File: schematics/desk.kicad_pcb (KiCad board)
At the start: 2 copper layers, 88 x 123 mm, 34 parts, among them K1 energized = UP (raises desk), K2 energized = DOWN (lowers desk), Q1 IRLZ44N, Q2 2N7000, Q3 2N7000, Q4 BC337, Q5 BC327, U1 LM2596HV 29V-5V, U2 ESP32_DevKitC, U3 74HC123 250ms, U5 ACS724xLCTR-05AB, U6 74HC08

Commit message: Shorten the bottom further: fix U5's inflated bounding box
Same bug as U2 had: U5's Value text ("ACS724xLCTR-05AB") was rotated
90 degrees and long enough to stretch its bounding box to 15.3mm tall,
when the real component (per its courtyard) is only ~3.6mm. This
introduced itself when I rotated U5 as a whole footprint earlier to
shrink cluster height - the rotation carried its text along for the
ride without me checking where the text landed afterward.

Un-rotated the value text, shrunk it slightly, and moved it to sit
under the part instead of trailing off below it. That row's height
bottleneck moves to R4/R5 (12.3mm) instead of U5 (15.3mm before this
fix) - the tallest item in that row drops by ~3mm, so the board
outline follows: bottom edge trimmed from 123mm to 120mm.

No re-routing needed - the closest existing track stayed well clear
of the new edge (max track y 116.6mm vs new 120mm edge). Just moved
the board outline and both ground zone boundaries to match, then
refilled. Same 30 expected DRC items as before (28 intentional
isolated-copper + 2 thermal-relief), 0 unconnected.

Worth a systematic check of every footprint's bounding box against
its courtyard if further compaction is wanted - this is the second
instance of the same failure mode (U2 was the first), and a handful
of other parts show smaller versions of it that weren't worth chasing
here (normal reference/value label margin, not a rotation artifact).
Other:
- board size 88 x 123 mm -> 88 x 120 mm
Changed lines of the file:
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@@
 		)
 		(property "Value" "ACS724xLCTR-05AB"
-			(at 0 20.55 90)
+			(at -4.754 8.9453 0)
 			(layer "F.Fab")
 			(effects
 				(font
-					(size 1 1)
+					(size 0.8 0.8)
 					(thickness 0.15)
 				)
@@
 	)
 	(gr_line
-		(start 0 123)
+		(start 0 120)
 		(end 0 0)
 		(stroke
@@
 	(gr_line
 		(start 88 0)
-		(end 88 123)
+		(end 88 120)
 		(stroke
 			(width 0.1)
@@
 	)
 	(gr_line
-		(start 88 123)
-		(end 0 123)
+		(start 88 120)
+		(end 0 120)
 		(stroke
 			(width 0.1)
@@
 		(polygon
 			(pts
-				(xy 2 2) (xy 86 2) (xy 86 121) (xy 2 121)
+				(xy 2 2) (xy 86 2) (xy 86 118) (xy 2 118)
 			)
 		)
@@
 		(polygon
 			(pts
-				(xy 2 2) (xy 86 2) (xy 86 121) (xy 2 121)
+				(xy 2 2) (xy 86 2) (xy 86 118) (xy 2 118)
 			)
 		)

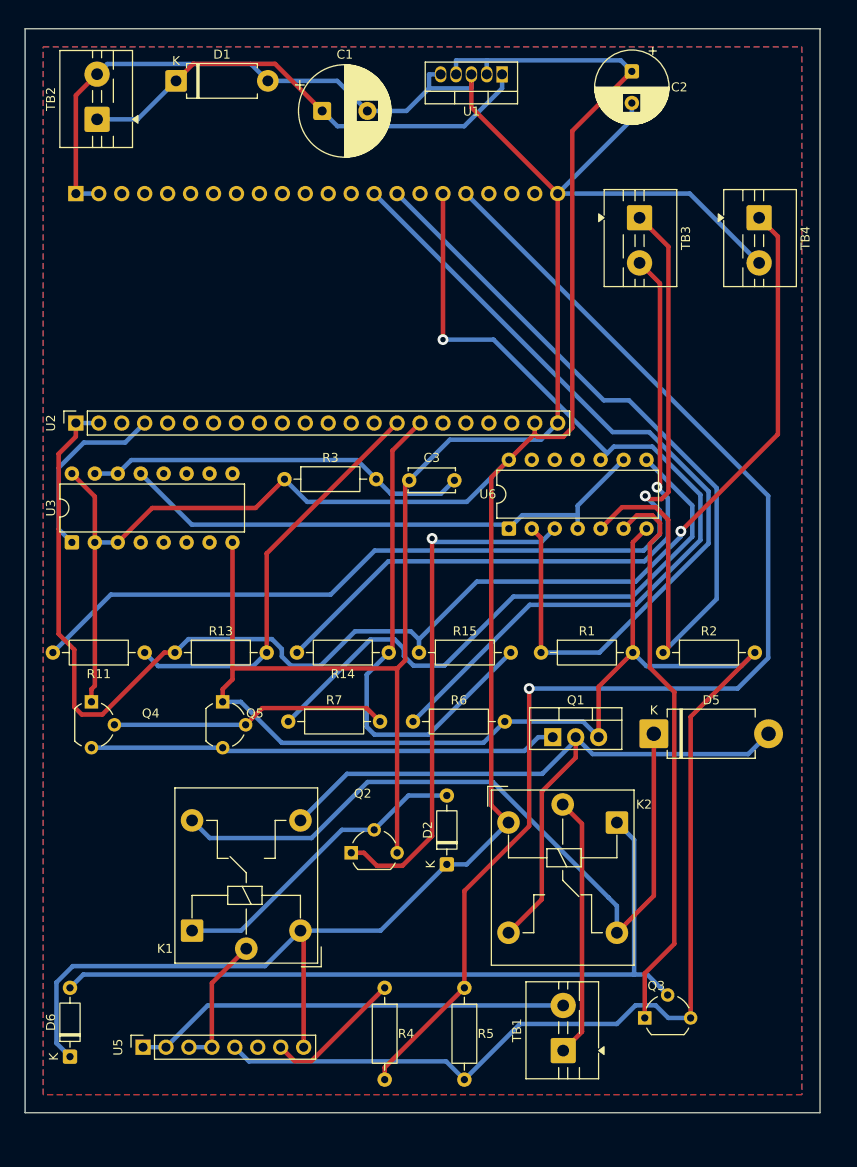
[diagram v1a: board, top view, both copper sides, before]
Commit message: Give R11 more edge clearance, clean up U3's label overhang
R11's left leg copper sat only 2.275mm from the board edge - the
tightest of any part on the board (everything else on the left margin
had 4mm+). Every other part in that row (R11/R13/R14/R15/R1/R2) had
6.2mm of unused width to its right before the board edge, so shifted
the whole row 1.7mm right: R11 now has 3.975mm of clearance, matching
the rest of the board, at zero cost to the layout.

Also did the full sweep for the U2/U5 text-overhang bug across every
footprint. Found one more real case (U3's "74HC123 250ms" value,
rotated 90 degrees, 12.8mm vs a 9.8mm courtyard) and cleaned it up,
though it doesn't change the board outline - U6 (18mm) is still the
taller item in that row. TB1-TB4's rotated "X pair" values looked
similar at a glance but turned out fine on inspection (bbox barely
exceeds their courtyard). Everything else's overhang is normal
reference/value label margin, not the rotation artifact.

Re-routed from scratch (moving R11's row moves real copper, so the
previous route no longer applied) and refilled both zones with the
same settings as the last two commits (0.4mm clearance, 0.3mm thermal
gap, island removal: never). 5 vias (down from 6 - shorter, more
direct routing after the shift). Same expected DRC profile: 0
unconnected, all violations are intentional isolated-copper/
starved-thermal from keeping disconnected mill fill.
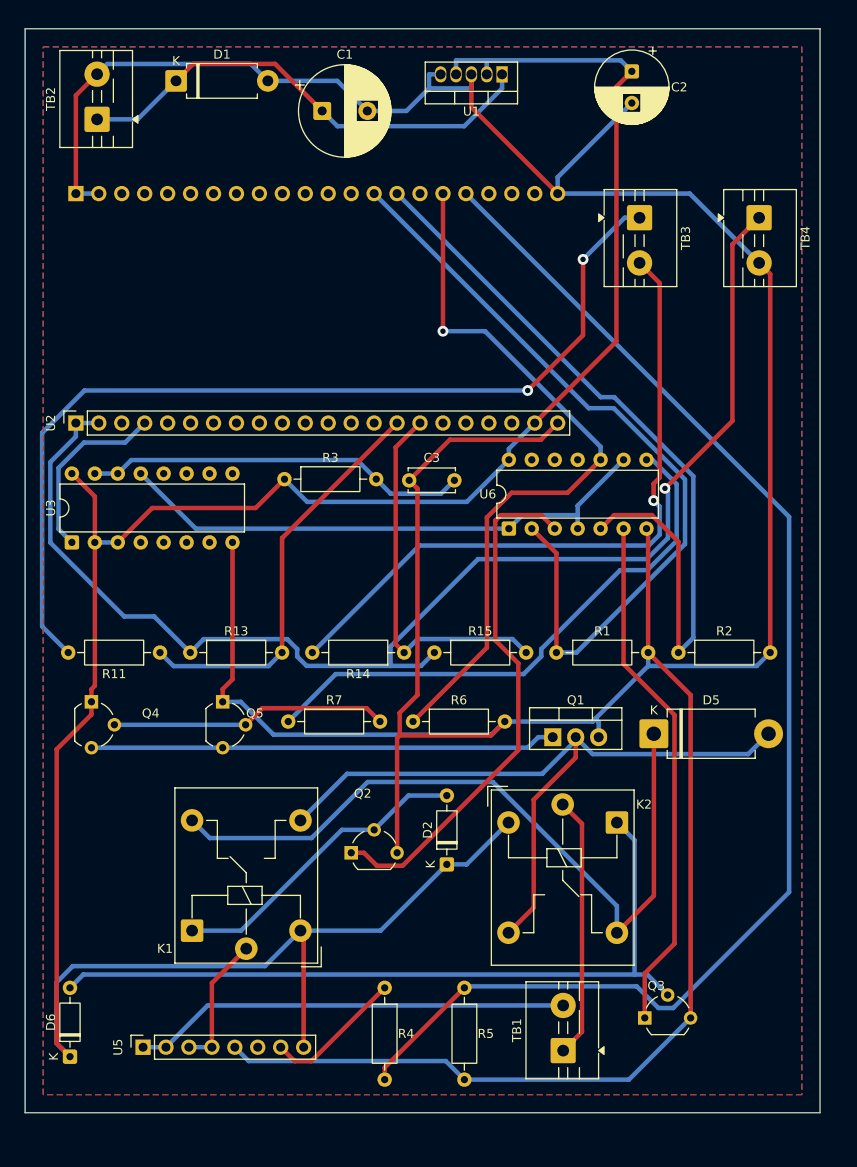
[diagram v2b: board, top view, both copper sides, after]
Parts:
- moved R15 1.70 mm to (45.3, 69.1)
- moved R2 1.70 mm to (72.3, 69.1)
- moved R11 1.70 mm to (14.9, 69.1)
- moved R13 1.70 mm to (18.3, 69.1)
- moved R1 1.70 mm to (58.8, 69.1)
- moved R14 1.70 mm to (42.0, 69.1)
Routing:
- net PWM: track 98.6 -> 80.6 mm
- net SW_DN: track 56.2 -> 41.7 mm
- net +3V3: track 156.9 -> 145.2 mm
- net GND: track 429.4 -> 438.4 mm
- net Net-(TB3-Pin_1): track 112.3 -> 106.4 mm, vias 1 -> 2
- net DIR_A: track 94.1 -> 88.7 mm
- net ISENSE: track 143.1 -> 148.3 mm, vias 1 -> 0
- net Net-(Q3-G): track 62.7 -> 57.9 mm
- net DIR_B: track 93.5 -> 88.7 mm
- net Net-(R7-Pad1): track 66.7 -> 62.5 mm
- net +5V: track 274.4 -> 270.6 mm
- net Net-(TB3-Pin_2): track 78.3 -> 75.4 mm
- net SW_UP: track 46.1 -> 45.4 mm
- net Net-(Q2-G): track 58.2 -> 58.3 mm, vias 1 -> 0

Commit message: Fix U2's row-2 pin mirroring - critical footprint bug
The custom DevKitC footprint numbered its second row of pins (23-44)
in the same top-to-bottom direction as row 1. Real 2-row DIP-style
headers - confirmed against Espressif's own official ESP32-S3-DevKitC
footprint, fetched directly from github.com/espressif/kicad-libraries -
number row 2 bottom-to-top: pin 23 sits across from pin 22, pin 44
across from pin 1. Every row-2 pin in this design was therefore wired
to its mirror-image physical position.

Impact: DIR_A, DIR_B, PWM, and ISENSE - four of this design's five
critical control signals - all live on row 2. A real ESP32-S3-DevKitC
plugged into a board built from the old footprint would have every one
of those four signals landing on the wrong physical socket pin.

This was flagged by inspection (a suspected pin count matched against
the schematic symbol's own pin table), not by DRC or ERC - neither
tool can catch this class of bug, since the netlist only ties nets to
pin *numbers*; a footprint with correct numbers at swapped physical
positions still reports as fully connected.

Fix keeps the 25.4mm row spacing (confirmed by direct measurement of
the real board - Espressif's official footprint uses 22.86mm, a
different DevKitC width variant, so wasn't adopted wholesale), and
carries over only the correct row-2 numbering *direction*. Also
replaced the placeholder-stub courtyard with one sized to the real
2-row footprint extent.

Tried adding per-pin GPIO-name silkscreen labels for hand-assembly
clarity, but they don't fit legally: even shortened names need ~3.8mm
of run length at the board's 0.8mm minimum silk text height, well over
the 2.54mm pin pitch. Dropped rather than fight it - not worth the
complexity for a nice-to-have.

Re-routed from scratch (all row-2 copper moved) and refilled both
zones with the same settings as recent commits. Board grew slightly
(88x120mm -> 90x124mm) since the corrected footprint's real courtyard
is bigger than the placeholder 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
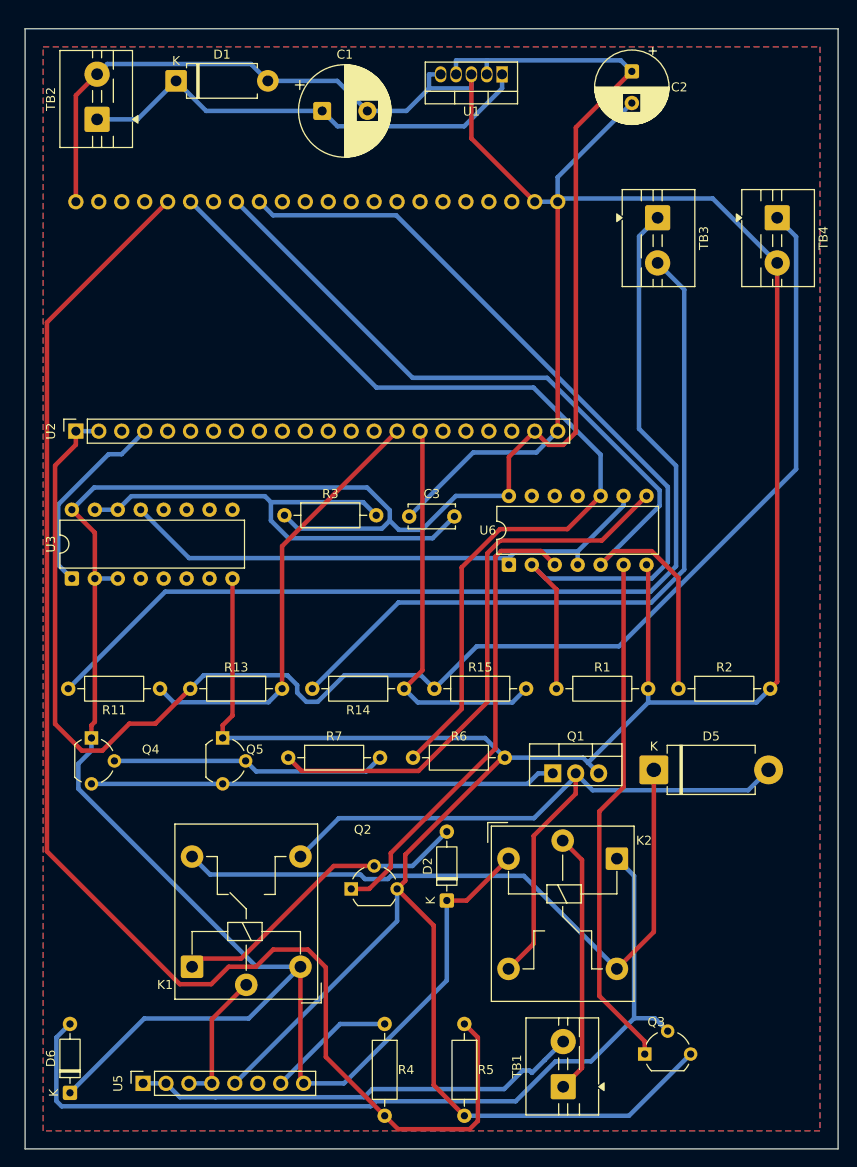
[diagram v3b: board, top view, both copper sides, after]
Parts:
- U2: footprint local:DevKitC_2x22_P2.54mm_1in_row -> DevKitC_2x22_P2.54mm_1in_row
- moved C3 4.00 mm to (42.5, 54.0)
- moved D2 4.00 mm to (46.7, 96.5)
- moved D5 4.00 mm to (69.6, 82.0)
- moved D6 4.00 mm to (4.97, 117.8)
- moved K1 4.00 mm to (18.5, 103.8)
- moved K2 4.00 mm to (65.5, 91.9)
- moved Q1 4.00 mm to (58.4, 82.4)
- moved Q2 4.00 mm to (36.1, 95.2)
- moved Q3 4.00 mm to (68.6, 113.5)
- moved Q4 4.00 mm to (7.34, 78.5)
- moved Q5 4.00 mm to (21.9, 78.5)
- moved R1 4.00 mm to (58.8, 73.1)
- moved R11 4.00 mm to (14.9, 73.1)
- moved R13 4.00 mm to (18.3, 73.1)
- moved R14 4.00 mm to (42.0, 73.1)
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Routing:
- net +5V: track 270.6 -> 296.4 mm
- net PWM: track 80.6 -> 103.5 mm, vias 1 -> 0
- net +3V3: track 145.2 -> 164.9 mm, vias 1 -> 0
- net Net-(D6-A): track 85.4 -> 100.2 mm
- net GND: track 438.4 -> 423.9 mm
- net Net-(U3A-Cext): track 42.6 -> 56.8 mm
- net ISENSE: track 148.3 -> 158.6 mm
- net DIR_A: track 88.7 -> 97.9 mm
- net Net-(TB3-Pin_1): track 106.4 -> 114.0 mm, vias 2 -> 0
- net VSW: track 82.8 -> 76.2 mm
- net Net-(TB3-Pin_2): track 75.4 -> 81.8 mm, vias 1 -> 0
- net Net-(Q2-G): track 58.3 -> 52.0 mm
- net DIR_B: track 88.7 -> 93.8 mm
- net SW_UP: track 45.4 -> 48.5 mm
- net SW_DN: track 41.7 -> 44.2 mm
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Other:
- board size 88 x 120 mm -> 90 x 124 mm

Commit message: Relocate D5/R2 into the unused U6-row space, stack TB3/TB4
Investigated the "move K1/K2 left for D5/R2" idea properly: appending
D5+R2 (rotated) directly after K2 needs ~18.5mm more linear space than
K2's row had, which would have grown the board to 101.8mm wide even
after TB3/TB4 stacking - net worse, not better. Rejected that placement
once the numbers were in hand.

The actual unused space was pointed out directly: the region right of
U6 (which ends at x=74.2) down through where the rocker row's R1 ends
(x=70.0) was completely empty - about 15.85 x 25.7mm, never used by
anything. D5 (rotated 90) fits right after U6; R2 (rotated 90) stacks
below it, using height that opened up once R2 left the rocker row.

Also stacked TB4 under TB3 at the board's right edge as asked, freeing
U2's row from needing to fit a second connector beside TB3.

Net effect, verified by actual bounding-box measurement rather than
estimate: true footprint extent drops to 84.8 x 121.1mm (was 89.2 x
122.2mm). Board outline set to 87x123mm (down from 90x124mm). The
switch/FET row also got 1.1mm shorter (Q1, not D5, is now its tallest
member), cascaded through every row below it.

K1/Q2/D2/K2 were NOT moved - once D5/R2 found a real home elsewhere,
compressing that row bought nothing further (confirmed: K2 already
fits comfortably inside the new 87mm width, so there was no reason to
touch it).

Re-routed from scratch, refilled both zones with the same settings as
recent commits. 0 vias, 0 unconnected, same accepted DRC profile
(isolated-copper + one starved-thermal from the deliberate mill-fill
decision).
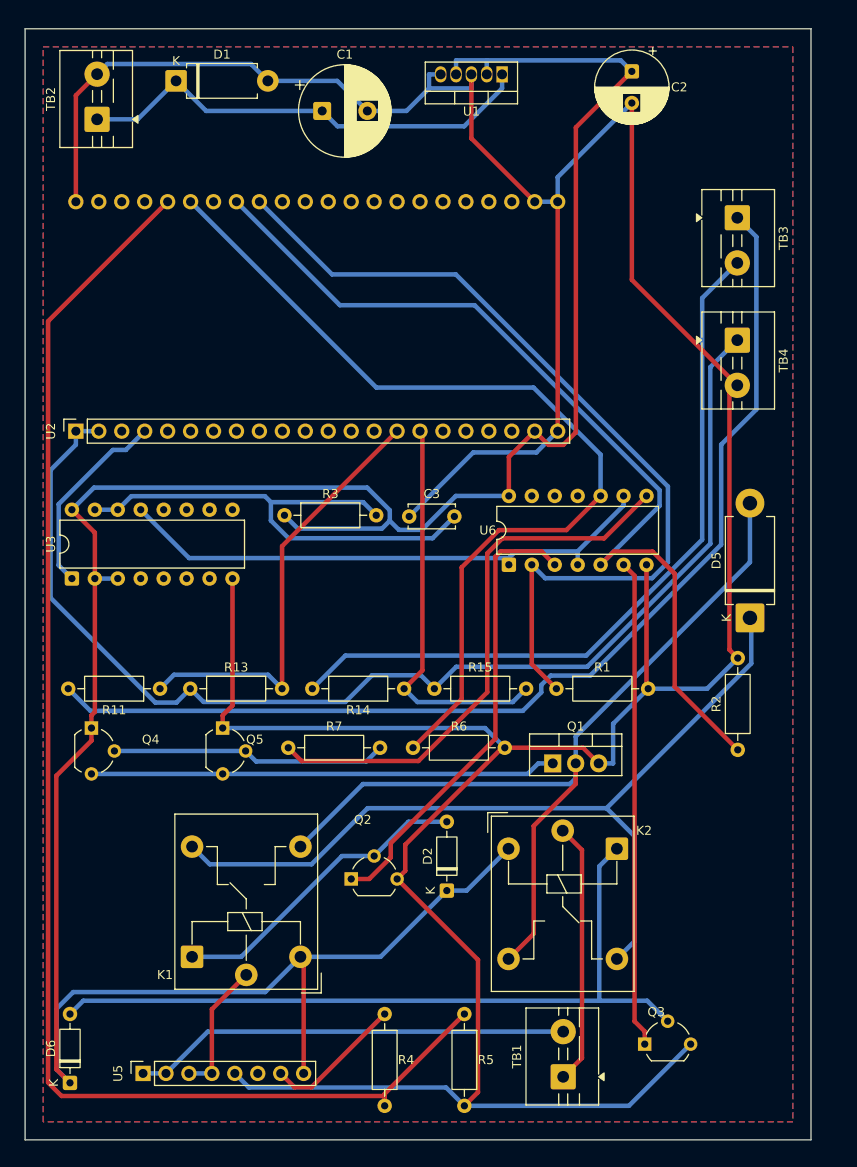
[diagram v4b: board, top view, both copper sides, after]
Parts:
- moved D5 19.9 mm to (80.2, 65.2), turned to 90 degrees
- moved TB4 14.3 mm to (78.8, 34.5)
- moved R2 9.43 mm to (78.9, 79.8), turned to 90 degrees
- moved TB3 8.82 mm to (78.8, 20.9)
- moved K2 1.10 mm to (65.5, 90.8)
- moved Q1 1.10 mm to (58.4, 81.3)
- moved R4 1.10 mm to (39.8, 109.1)
- moved R5 1.10 mm to (48.6, 109.1)
- moved TB1 1.10 mm to (59.6, 116.0)
- moved D2 1.10 mm to (46.7, 95.4)
- moved D6 1.10 mm to (4.97, 116.7)
- moved K1 1.10 mm to (18.5, 102.7)
- moved Q2 1.10 mm to (36.1, 94.1)
- moved Q3 1.10 mm to (68.6, 112.4)
- moved Q4 1.10 mm to (7.34, 77.4)
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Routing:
- net +3V3: track 164.9 -> 133.5 mm
- net VSW: track 76.2 -> 95.8 mm
- net Net-(D6-A): track 100.2 -> 85.4 mm
- net /MRET: track 82.2 -> 96.8 mm
- net GND: track 423.9 -> 411.9 mm
- net DIR_B: track 93.8 -> 103.2 mm
- net Net-(TB3-Pin_1): track 114.0 -> 120.1 mm
- net ISENSE: track 158.6 -> 154.7 mm
- net Net-(Q3-G): track 57.4 -> 54.0 mm
- net +5V: track 296.4 -> 294.6 mm
- net Net-(TB1-Pin_2): track 49.9 -> 48.4 mm
- net Net-(U5-VIOUT): track 14.2 -> 15.5 mm
- net Net-(Q2-G): track 52.0 -> 50.9 mm
- net Net-(R7-Pad1): track 62.5 -> 61.4 mm
- net PWM: track 103.5 -> 102.4 mm
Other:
- board size 90 x 124 mm -> 87 x 123 mm
